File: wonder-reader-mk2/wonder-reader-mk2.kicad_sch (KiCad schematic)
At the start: 33 parts, among them M1 Stepper_Motor_unipolar_5pin, M2 Stepper_Motor_bipolar, M3 Stepper_Motor_bipolar, M4 Stepper_Motor_bipolar, M5 Stepper_Motor_bipolar, M6 Stepper_Motor_bipolar, M7 Stepper_Motor_bipolar, SW1 SW_Push, SW2 SW_Push, SW3 SW_Push, SW4 SW_Push, SW5 SW_Push, SW6 Stepper_Limit, SW8 SW_SPST, U1 ESP32, U2 MAX98357A, U3 BQ297xy, U3 Vibration Motor, U5 ULN2003, U7 74HC595, U8 74HC595, U9 74HC595

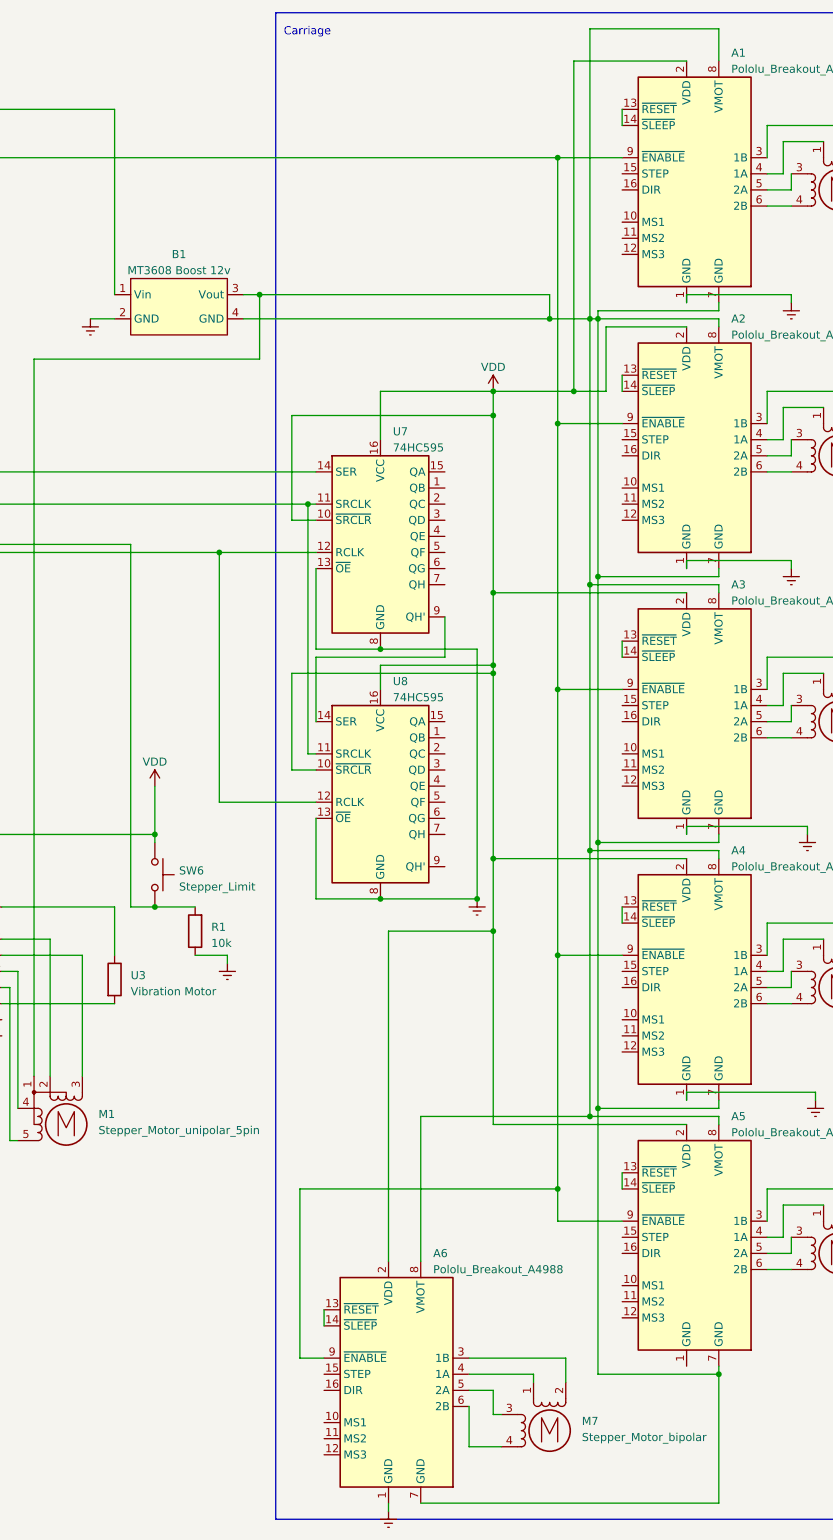
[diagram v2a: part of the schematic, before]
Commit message: Added new model for new carriage
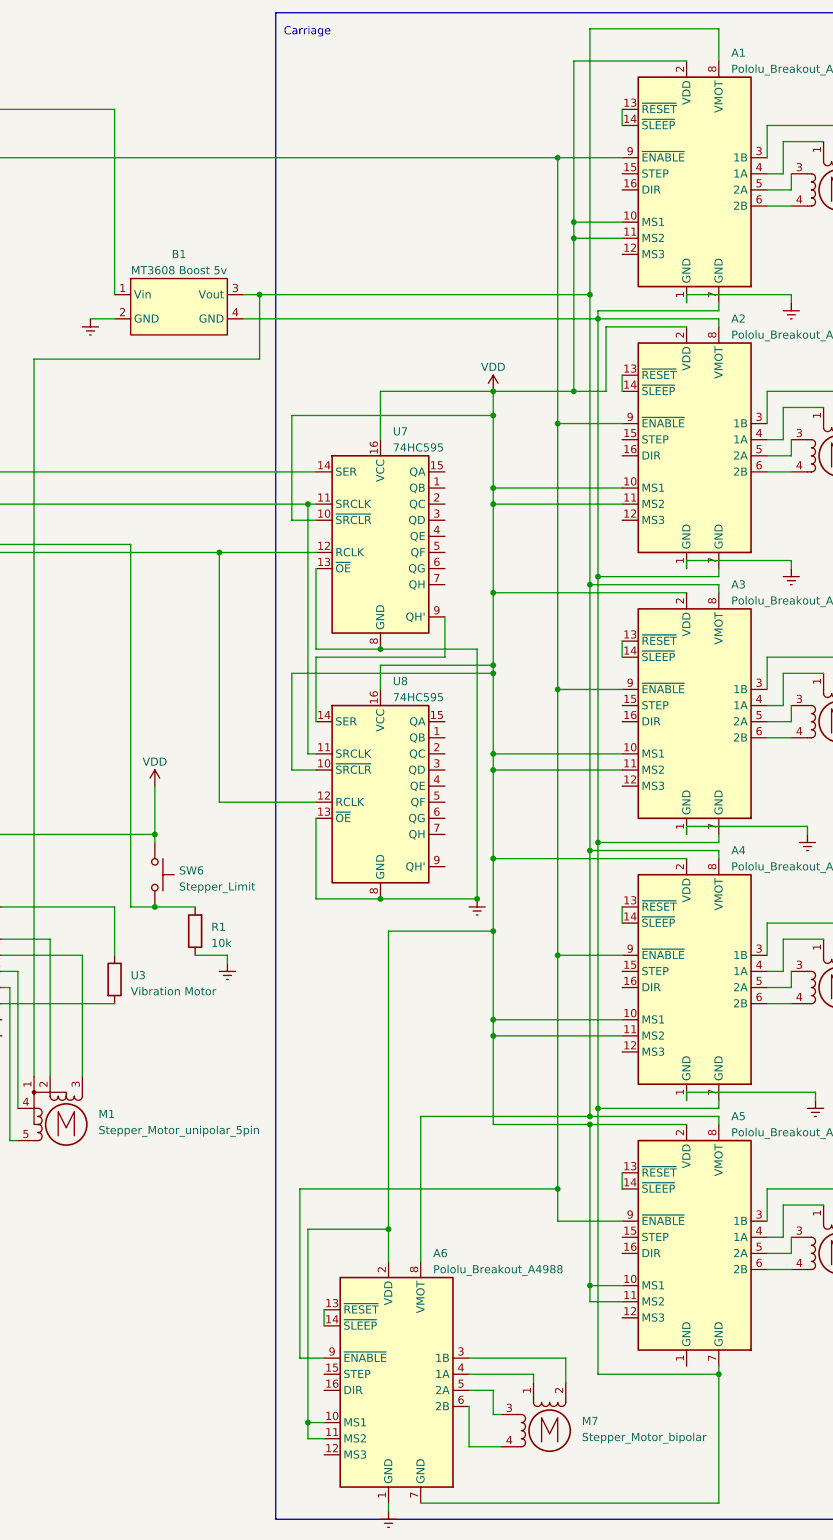
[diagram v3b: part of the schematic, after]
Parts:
- B1: value MT3608 Boost 12v -> MT3608 Boost 5v
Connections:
- net VDD: now also A1.10 (MS1), A1.11 (MS2), A2.10 (MS1), A2.11 (MS2), A3.10 (MS1), A3.11 (MS2), A4.10 (MS1), A4.11 (MS2), A5.10 (MS1), A5.11 (MS2), A6.10 (MS1), A6.11 (MS2)
- net at A1.7 (GND), A2.7 (GND), A2.8 (VMOT)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: no longer A1.8 (VMOT), A3.8 (VMOT), A4.8 (VMOT), A5.8 (VMOT), A6.8 (VMOT), B1.3 (Vout), M1.1
- new net: A1.8 (VMOT), A3.8 (VMOT), A4.8 (VMOT), A5.8 (VMOT), A6.8 (VMOT), B1.3 (Vout), M1.1

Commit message: Added cases and switches. Updated carriage load models and bearing brackets. Schematic update
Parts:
- removed U3: Vibration Motor, symbol Device:R
- added SW10, SW11, SW12, SW13, SW14, SW15, SW16, SW17, SW18, SW7, SW9: SW_Push, symbol Switch:SW_Push
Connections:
- net VDD: no longer A1.10 (MS1), A1.11 (MS2), A2.10 (MS1), A2.11 (MS2), A3.10 (MS1), A3.11 (MS2), A4.10 (MS1), A4.11 (MS2), A5.10 (MS1), A5.11 (MS2), A6.10 (MS1), A6.11 (MS2)
- net at SW3.1: now also SW1.1, SW2.1, SW4.1, U1.5 (SENSOR_VP/GPIO36/ADC1_CH0)
- net at SW3.2: now also U1.13 (32K_XN/GPIO33/ADC1_CH5), SW15.2, SW16.2, SW9.2
- net at U1.36 (GPIO23): now also SW1.2, SW5.2, SW11.2, SW12.2; no longer U5.5 (I5)
- net at U8.1 (QB): now also A5.16 (DIR)
- net at U8.15 (QA): now also A5.15 (STEP)
- net at U8.2 (QC): now also A6.15 (STEP)
- net at U8.3 (QD): now also A6.16 (DIR)
- net at A1.15 (STEP): now also U7.15 (QA)
- net at A1.16 (DIR): now also U7.1 (QB)
- net at SW5.1: now also U1.8 (SENSOR_VN/GPIO39/ADC1_CH3), SW10.1, SW7.1, SW9.1
- net at SW4.2: now also U1.12 (32K_XP/GPIO32/ADC1_CH4), SW10.2, SW17.2, SW18.2
- net at SW2.2: now also U1.16 (GPIO27/ADC2_CH7), SW13.2, SW14.2, SW7.2
- net at U1.10 (VDET_1/GPIO34/ADC1_CH6): now also SW11.1, SW13.1, SW15.1, SW17.1
- net at U1.11 (VDET_2/GPIO35/ADC1_CH7): now also SW12.1, SW14.1, SW16.1, SW18.1
- net at A3.15 (STEP): now also U7.4 (QE)
- net at A3.16 (DIR): now also U7.5 (QF)
- net at A4.15 (STEP): now also U7.6 (QG)
- net at A4.16 (DIR): now also U7.7 (QH)
- net at U7.2 (QC): now also A2.15 (STEP)
- net at U7.3 (QD): now also A2.16 (DIR)
- no-connect marks 0 -> 14
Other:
- moved on the sheet: SW1, SW2, SW3, SW4, SW5

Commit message: Added new pcb and more step files for mark 2. Renamed previous mark 2 to mark 1 and mark 1 to mark 0
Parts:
- removed A1, A2, A3, A4, A5, A6: Pololu_Breakout_A4988, Module:Pololu_Breakout-16_15.2x20.3mm, symbol Driver_Motor:Pololu_Breakout_A4988
- removed B1, B2: MT3608 Boost 5v, symbol Custom:MT3608 Boost
- removed BT1: Battery, symbol Device:Battery
- removed LS1: Speaker, symbol Device:Speaker
- removed M1: Stepper_Motor_unipolar_5pin, symbol Motor:Stepper_Motor_unipolar_5pin
- removed M2, M3, M4, M5, M6, M7: Stepper_Motor_bipolar, symbol Motor:Stepper_Motor_bipolar
- removed SW1, SW10, SW11, SW12, SW13, SW14, SW15, SW16, SW17, SW18, SW2, SW3, SW4, SW5, SW7, SW9: SW_Push, symbol Switch:SW_Push
- removed SW6: Stepper_Limit, symbol Switch:SW_Push
- removed SW8: SW_SPST, symbol Switch:SW_SPST
- removed U1: ESP32, symbol Espressif:ESP32
- removed U2: MAX98357A, symbol Custom:MAX98357A
- removed U3: BQ297xy, Package_SON:WSON-6_1.5x1.5mm_P0.5mm, symbol Battery_Management:BQ297xy
- removed U5: ULN2003, symbol Transistor_Array:ULN2003
- removed U7, U8, U9: 74HC595, symbol 74xx:74HC595
- added C1: 1000u, Capacitor_THT:C_Radial_D10.0mm_H16.0mm_P5.00mm, symbol Device:C
- added C2: 33u, Capacitor_THT:C_Radial_D5.0mm_H11.0mm_P2.00mm, symbol Device:C
- added H1, H2: MountingHole, MountingHole:MountingHole_2.2mm_M2, symbol Mechanical:MountingHole
- added J1: Conn_01x04_Pin, Connector_PinSocket_2.54mm:PinSocket_1x04_P2.54mm_Vertical, symbol Connector:Conn_01x04_Pin
- added J2, J4: Conn_01x02_Pin, Connector_PinHeader_2.54mm:PinHeader_1x02_P2.54mm_Vertical, symbol Connector:Conn_01x02_Pin
- added J5: Conn_01x08_Pin, Connector_PinHeader_2.54mm:PinHeader_1x08_P2.54mm_Vertical, symbol Connector:Conn_01x08_Pin
- added J6: Conn_01x04_Pin, Connector_PinHeader_2.54mm:PinHeader_1x04_P2.54mm_Vertical, symbol Connector:Conn_01x04_Pin
- added J7: Conn_01x10_MountingPin, Connector_FFC-FPC:Hirose_FH12-10S-0.5SH_1x10-1MP_P0.50mm_Horizontal, symbol Connector_Generic_MountingPin:Conn_01x10_MountingPin
- added R2, R3, R4, R5: 10K, Resistor_SMD:R_0805_2012Metric, symbol Device:R
- added U1: ESP32-DevKitC, Espressif:ESP32-DevKitC, symbol Espressif:ESP32-DevKitC
- added U2: A4988_STEPPER_MOTOR_DRIVER_CARRIER, A4988_STEPPER_MOTOR_DRIVER_CARRIER:MODULE_A4988_STEPPER_MOTOR_DRIVER_CARRIER, symbol A4988_STEPPER_MOTOR_DRIVER_CARRIER:A4988_STEPPER_MOTOR_DRIVER_CARRIER
- added U3: AMS1117-3.3, Package_TO_SOT_SMD:SOT-223-3_TabPin2, symbol Regulator_Linear:AMS1117-3.3
- added U5: 74HC595, Package_DIP:DIP-16_W7.62mm, symbol 74xx:74HC595
- added U6: MAX98357A, Custompretty:MAX98357A, symbol Custom:MAX98357A
- R1: value 10k -> 10K; footprint (none) -> Resistor_SMD:R_0805_2012Metric
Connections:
- net GND: now reaches R1.2
- net GND: now also C1.2, C2.1, J2.2 (Pin_2), J6.3 (Pin_3), J7.10 (Pin_10), R2.1, R3.1, R4.1, R5.1, U1.32 (GND), U1.38 (GND), U2.15 (GND), U2.9 (GND), U3.1 (GND), U5.13 (~{OE}), U5.8 (GND), U6.2 (GND), U6.3 (GAIN)
- net Earth renamed Limit_In
- net Limit_In: now also J4.2 (Pin_2), U1.33 (GPIO21)
- new net: J1.1 (Pin_1), U2.14 (2B)
- new net: J1.2 (Pin_2), U2.13 (2A)
- new net: J1.3 (Pin_3), U2.12 (1A)
- new net: J1.4 (Pin_4), U2.11 (1B)
- new net: J7.1 (Pin_1), U5.15 (QA)
- new net: J7.2 (Pin_2), U5.1 (QB)
- new net: J7.3 (Pin_3), U5.2 (QC)
- new net: J7.4 (Pin_4), U5.3 (QD)
- new net: J7.5 (Pin_5), U5.4 (QE)
- new net: J7.6 (Pin_6), U5.5 (QF)
- new net: J7.7 (Pin_7), U5.6 (QG)
- new net: U2.5 (~{RESET}), U2.6 (~{SLEEP})
- new net +12V: C1.1, J2.1 (Pin_1), J7.9 (Pin_9), U2.16 (VMOT), U3.3 (VI)
- new net +3.3V: C2.2, J4.1 (Pin_1), J6.4 (Pin_4), J7.8 (Pin_8), U1.1 (3V3), U2.10 (VDD), U3.2 (VO), U5.10 (~{SRCLR}), U5.16 (VCC), U6.1 (VIN)
- new net BCLK: U1.10 (DAC_2/ADC2_CH9/GPIO26), U6.5 (BCLK)
- new net DIN: U1.37 (GPIO23), U6.4 (DIN)
- new net Dir: U1.31 (GPIO19), U2.8 (DIR)
- new net LRC: U1.9 (DAC_1/ADC2_CH8/GPIO25), U6.6 (LRC)
- new net Matrix_I1: J5.4 (Pin_4), R5.2, U1.6 (VDET_2/GPIO35/ADC1_CH7)
- new net Matrix_I2: J5.3 (Pin_3), R4.2, U1.5 (VDET_1/GPIO34/ADC1_CH6)
- new net Matrix_I3: J5.2 (Pin_2), R2.2, U1.4 (SENSOR_VN/GPIO39/ADC1_CH3)
- new net Matrix_I4: J5.1 (Pin_1), R3.2, U1.3 (SENSOR_VP/GPIO36/ADC1_CH0)
- new net Matrix_O1: J5.8 (Pin_8), U1.24 (ADC2_CH2/*GPIO2)
- new net Matrix_O2: J5.5 (Pin_5), U1.11 (ADC2_CH7/GPIO27)
- new net Matrix_O3: J5.6 (Pin_6), U1.8 (32K_XN/GPIO33/ADC1_CH5)
- new net Matrix_O4: J5.7 (Pin_7), U1.7 (32K_XP/GPIO32/ADC1_CH4)
- new net RCLK: U1.28 (GPIO17), U5.12 (RCLK)
- new net RX: J6.2 (Pin_2), U1.34 (U0RXD/GPIO3)
- new net SER: U1.29 (*GPIO5), U5.14 (SER)
- new net SRCLK: U1.27 (GPIO16), U5.11 (SRCLK)
- new net Step: U1.30 (GPIO18), U2.7 (STEP)
- new net Stepper_Ena: U1.36 (GPIO22), U2.1 (~{ENABLE})
- new net TX: J6.1 (Pin_1), U1.35 (U0TXD/GPIO1)
- no-connect marks 14 -> 22
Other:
- note added: "For production, probably needs its own power supply"
- note added: "No need capacitor in VI to GND because already in a4988"
- note removed: "20BYJ46 vs 28BYJ-48 Note: 28BYJ-48 pin order is 12345 where 1 is the red wire 20BYJ-48 pin order is 12543 where 3 is the brown wire"
- note removed: "AccelStepper Note: For unipolar stepper 4 pins, pin 2 and 3 should be switched if going by order of wire"
- note removed: "Carriage"
- note removed: "Into ESP-32 VIN"
- company: Team Lily -> Project Lily
- title: Wonder Reader Mk2 -> Wonder Reader 2 Mainboard

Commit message: PCB and new models for mark 2
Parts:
- removed J7: Conn_01x10_MountingPin, Connector_FFC-FPC:Hirose_FH12-10S-0.5SH_1x10-1MP_P0.50mm_Horizontal, symbol Connector_Generic_MountingPin:Conn_01x10_MountingPin
- added A1, A2, A3: Pololu_Breakout_A4988, Module:Pololu_Breakout-16_15.2x20.3mm, symbol Driver_Motor:Pololu_Breakout_A4988
- added H3, H4, H5, H6: MountingHole, MountingHole:MountingHole_2.2mm_M2, symbol Mechanical:MountingHole
- added J10, J11, J9: Conn_01x04_Pin, Connector_PinHeader_2.54mm:PinHeader_1x04_P2.54mm_Vertical, symbol Connector:Conn_01x04_Pin
- added J12, J8: Conn_01x12_MountingPin, Connector_FFC-FPC:Hirose_FH12-12S-0.5SH_1x12-1MP_P0.50mm_Horizontal, symbol Connector_Generic_MountingPin:Conn_01x12_MountingPin
- added J14, J7: Conn_01x05_Pin, Connector_PinHeader_2.54mm:PinHeader_1x05_P2.54mm_Vertical, symbol Connector:Conn_01x05_Pin
- added J3: Conn_01x10_Pin, Connector_PinHeader_2.54mm:PinHeader_1x10_P2.54mm_Vertical, symbol Connector:Conn_01x10_Pin
- J1: footprint Connector_PinSocket_2.54mm:PinSocket_1x04_P2.54mm_Vertical -> Connector_PinHeader_2.54mm:PinHeader_1x04_P2.54mm_Vertical
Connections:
- net +12V: now also J3.2 (Pin_2)
- net +3.3V: now also J3.3 (Pin_3)
- net Dir: now also U1.30 (GPIO18); no longer U1.31 (GPIO19)
- net GND: now also A1.1 (GND), A1.7 (GND), A2.1 (GND), A2.7 (GND), A3.1 (GND), A3.7 (GND), J14.1 (Pin_1), J3.1 (Pin_1)
- net Matrix_O2: now also J5.7 (Pin_7); no longer J5.5 (Pin_5)
- net Matrix_O4: now also J5.5 (Pin_5); no longer J5.7 (Pin_7)
- net SER: now also U5.11 (SRCLK); no longer U5.14 (SER)
- net SRCLK: now also U5.14 (SER); no longer U5.11 (SRCLK)
- net Step: now also U1.31 (GPIO19); no longer U1.30 (GPIO18)
- net at U5.15 (QA): now also J3.10 (Pin_10)
- net at U5.1 (QB): now also J3.9 (Pin_9)
- net at U5.2 (QC): now also J3.8 (Pin_8)
- net at U5.3 (QD): now also J3.7 (Pin_7)
- net at U5.4 (QE): now also J3.6 (Pin_6)
- net at U5.5 (QF): now also J3.5 (Pin_5)
- net at U5.6 (QG): now also J3.4 (Pin_4)
- new net: J12.1 (Pin_1), J9.1 (Pin_1)
- new net: J10.2 (Pin_2), J12.10 (Pin_10)
- new net: J10.3 (Pin_3), J12.11 (Pin_11)
- new net: J10.4 (Pin_4), J12.12 (Pin_12)
- new net: J12.2 (Pin_2), J9.2 (Pin_2)
- new net: J12.3 (Pin_3), J9.3 (Pin_3)
- new net: J12.4 (Pin_4), J9.4 (Pin_4)
- new net: J11.1 (Pin_1), J12.5 (Pin_5)
- new net: J11.2 (Pin_2), J12.6 (Pin_6)
- new net: J11.3 (Pin_3), J12.7 (Pin_7)
- new net: J11.4 (Pin_4), J12.8 (Pin_8)
- new net: J10.1 (Pin_1), J12.9 (Pin_9)
- new net: A1.8 (VMOT), A2.8 (VMOT), A3.8 (VMOT), J14.2 (Pin_2)
- new net: A1.2 (VDD), A2.2 (VDD), A3.2 (VDD), J14.3 (Pin_3)
- new net: A1.9 (~{ENABLE}), A2.9 (~{ENABLE}), A3.9 (~{ENABLE}), J14.4 (Pin_4)
- new net: A3.15 (STEP), J14.5 (Pin_5)
- new net: A3.13 (~{RESET}), A3.14 (~{SLEEP})
- new net: A3.16 (DIR), J7.1 (Pin_1)
- new net: A3.3 (1B), J8.1 (Pin_1)
- new net: A3.4 (1A), J8.2 (Pin_2)
- new net: A3.5 (2A), J8.3 (Pin_3)
- new net: A3.6 (2B), J8.4 (Pin_4)
- new net: A1.4 (1A), J8.10 (Pin_10)
- new net: A1.5 (2A), J8.11 (Pin_11)
- new net: A1.6 (2B), J8.12 (Pin_12)
- new net: A2.3 (1B), J8.5 (Pin_5)
- new net: A2.4 (1A), J8.6 (Pin_6)
- new net: A2.5 (2A), J8.7 (Pin_7)
- new net: A2.6 (2B), J8.8 (Pin_8)
- new net: A1.3 (1B), J8.9 (Pin_9)
- new net: A1.15 (STEP), J7.2 (Pin_2)
- new net: A1.16 (DIR), J7.3 (Pin_3)
- new net: A2.15 (STEP), J7.4 (Pin_4)
- new net: A2.16 (DIR), J7.5 (Pin_5)
- new net: A1.13 (~{RESET}), A1.14 (~{SLEEP})
- new net: A2.13 (~{RESET}), A2.14 (~{SLEEP})
- no-connect marks 22 -> 32
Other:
- moved on the sheet: C2, J2, U3
